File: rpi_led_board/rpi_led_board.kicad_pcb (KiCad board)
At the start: 2 copper layers, 65 x 22.4 mm, 67 parts, among them P1 Conn_02x20_Odd_Even

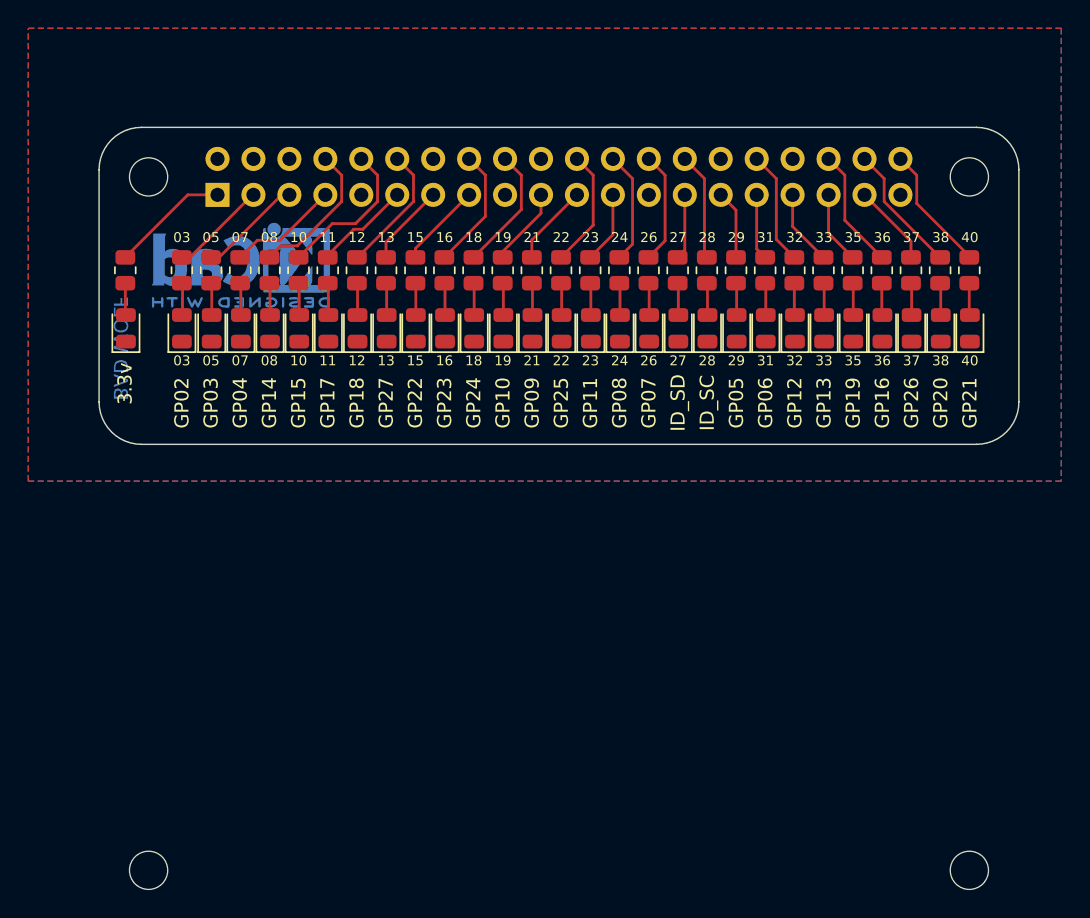
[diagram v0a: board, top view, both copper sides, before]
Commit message: updated silkscreen
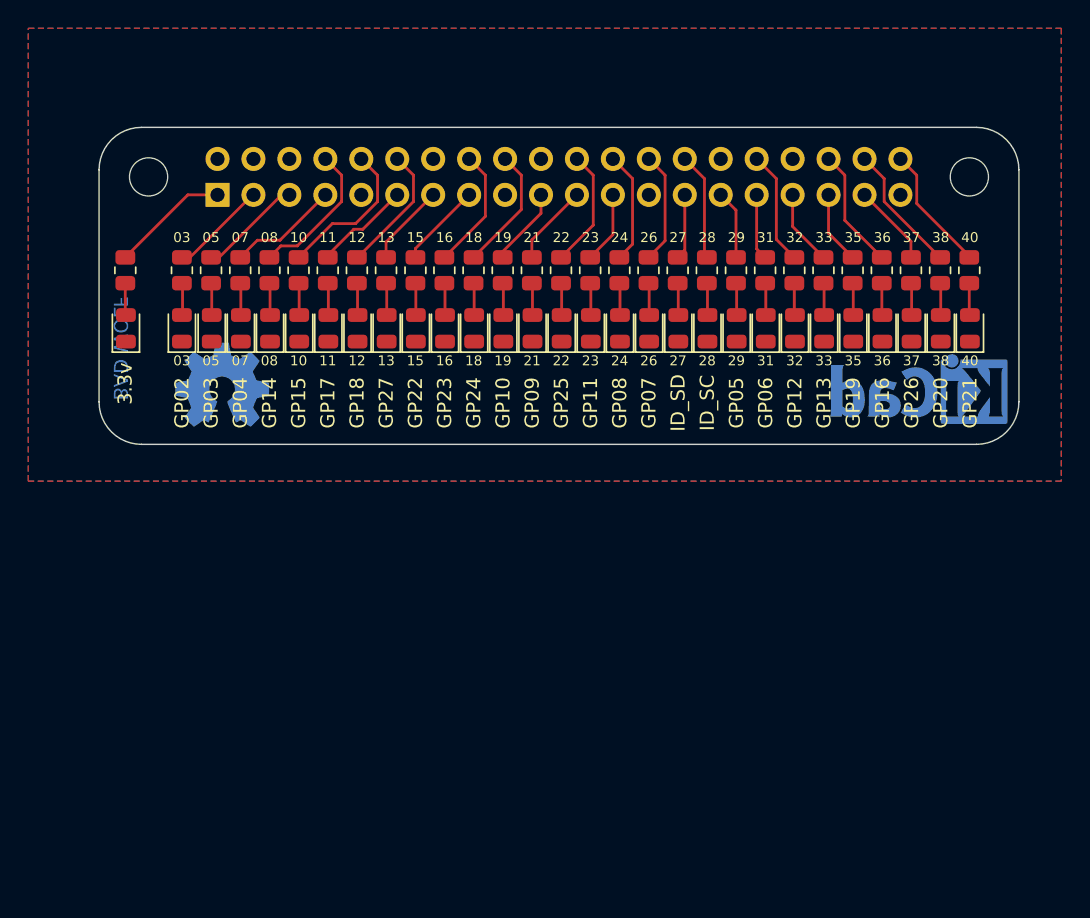
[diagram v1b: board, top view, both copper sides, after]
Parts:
- removed MK3, MK4: M2.5, MountingHole:MountingHole_2.7mm_M2.5
- removed the REF** at (210.0, 103.7)
- added REF**: OSHW-Symbol_6.7x6mm_Copper, Symbol:OSHW-Symbol_6.7x6mm_Copper, B.Cu at (208.7, 112.2)
- added REF**: KiCad-Logo_5mm_Copper, Symbol:KiCad-Logo_5mm_Copper, B.Cu at (257.9, 113.0)
- moved G*** 1.45 mm to (240.3, 105.8)
- moved G*** 1.26 mm to (226.4, 105.9)
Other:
- board text added: "Version 1.0 Copyright 2022 akuker"
